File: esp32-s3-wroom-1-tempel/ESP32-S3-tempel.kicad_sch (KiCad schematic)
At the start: 33 parts, among them J1 USB, J2 USB2UART, J3 West, J4 East, J5 Nort, J6 South, Q1 SS8050, Q2 SS8050, SW1 RST, SW2 Boot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

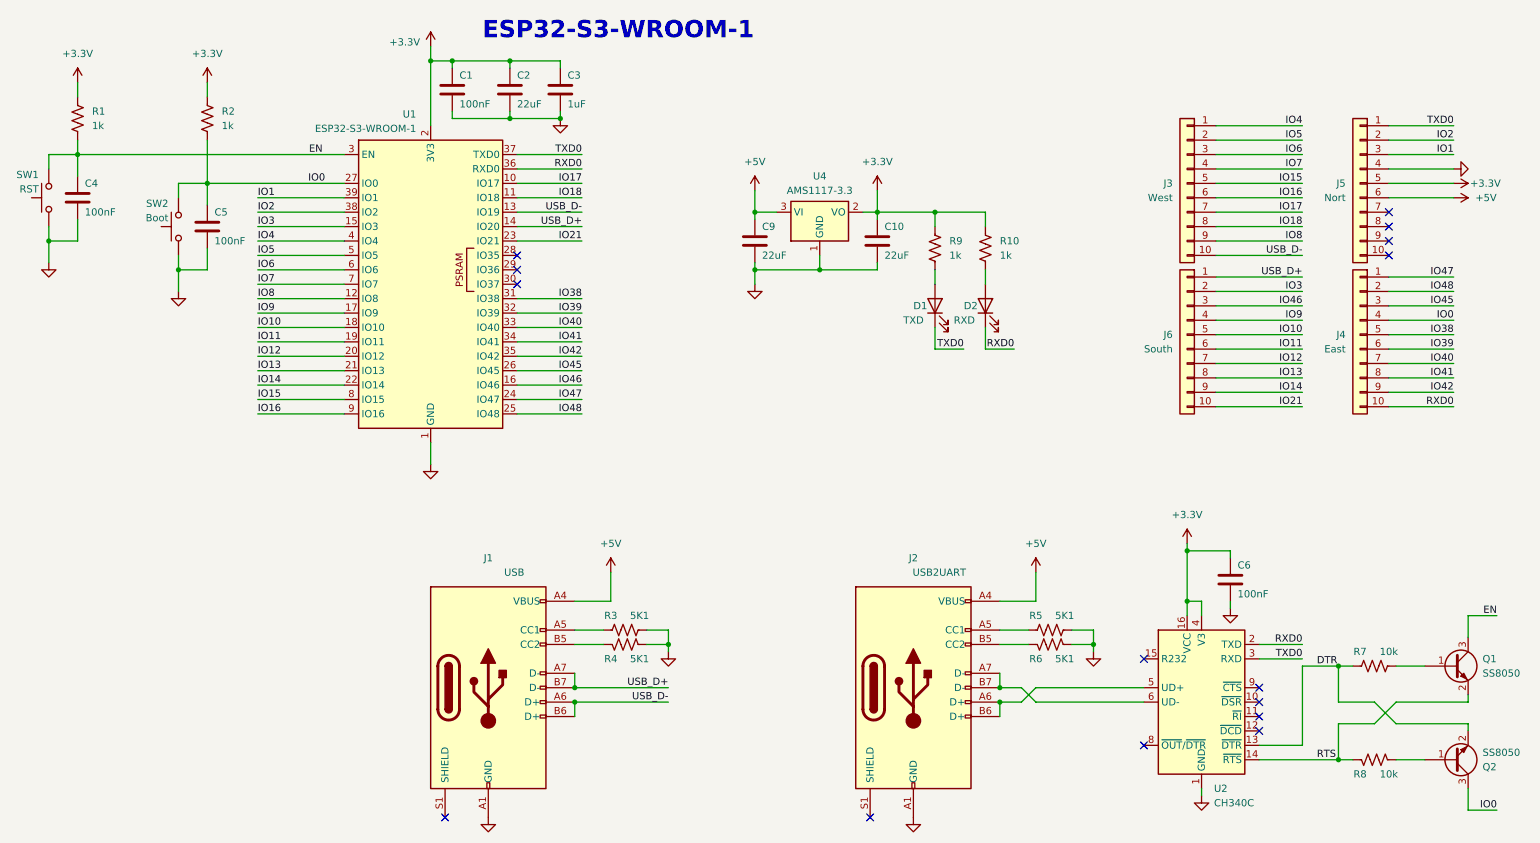
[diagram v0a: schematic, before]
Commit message: feat: make esp32-s3-wroom-1 temple route more ticker
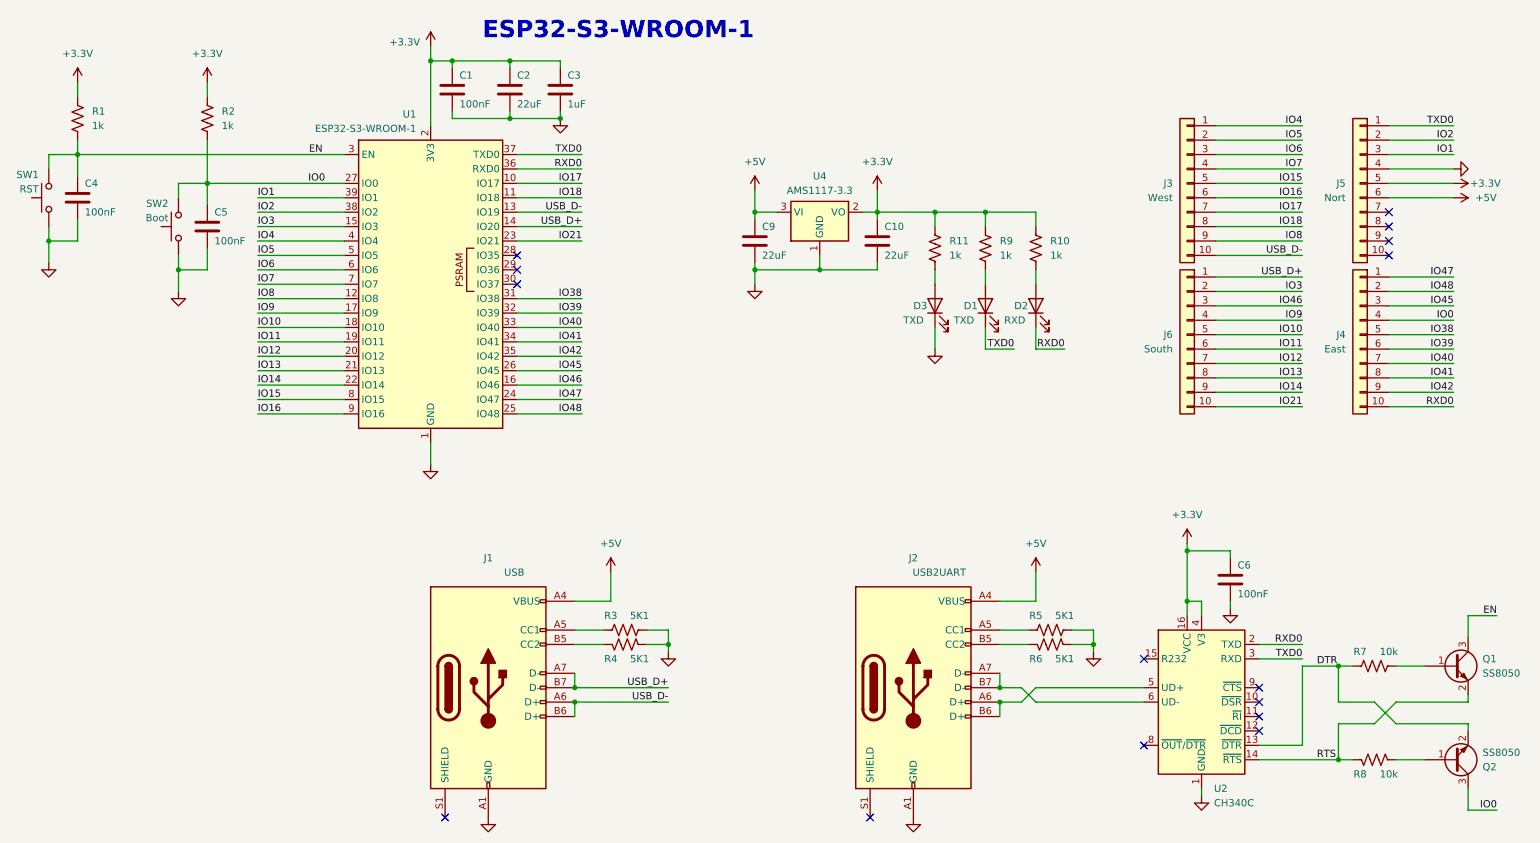
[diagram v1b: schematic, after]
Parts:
- added D3: TXD, LED_SMD:LED_1206_3216Metric_Pad1.42x1.75mm_HandSolder, symbol Device:LED
- added R11: 1k, Resistor_SMD:R_0805_2012Metric_Pad1.20x1.40mm_HandSolder, symbol Device:R_US
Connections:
- net +3.3V: now also R11.1
- net GND: now also D3.1 (K)
- new net: D3.2 (A), R11.2
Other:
- moved on the sheet: D1, D2, R10, R9
